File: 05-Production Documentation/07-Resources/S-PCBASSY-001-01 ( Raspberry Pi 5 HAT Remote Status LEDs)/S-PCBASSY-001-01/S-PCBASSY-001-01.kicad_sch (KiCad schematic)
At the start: 0 parts

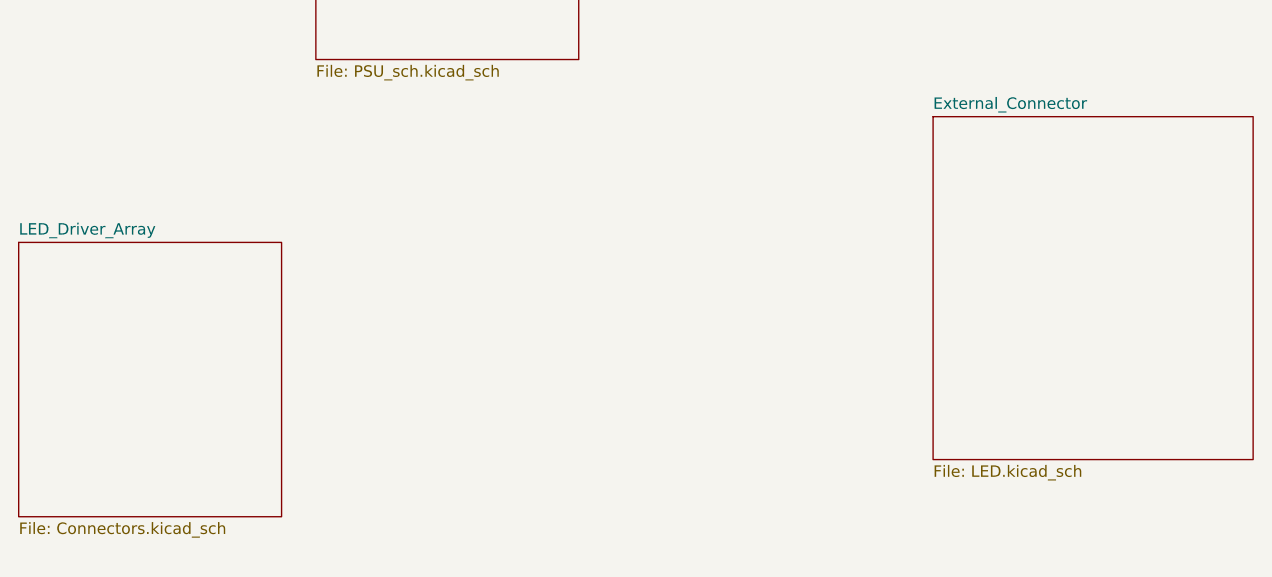
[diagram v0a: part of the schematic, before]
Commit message: Connector added with TVS still need to add polarity Protection
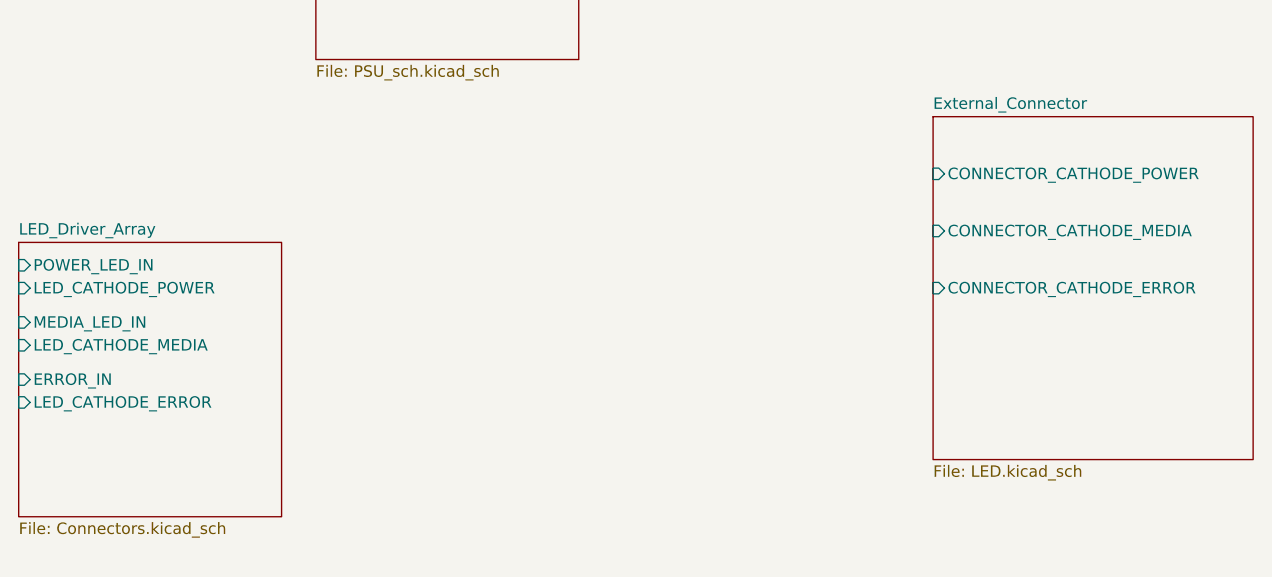
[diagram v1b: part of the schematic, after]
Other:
- sheet External_Connector ports: added CONNECTOR_CATHODE_ERROR, CONNECTOR_CATHODE_MEDIA, CONNECTOR_CATHODE_POWER; removed none
- sheet LED_Driver_Array ports: added ERROR_IN, LED_CATHODE_ERROR, LED_CATHODE_MEDIA, LED_CATHODE_POWER, MEDIA_LED_IN, POWER_LED_IN; removed none
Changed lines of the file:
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@@
+			)
+		)
+		(pin "LED_CATHODE_MEDIA" input
+			(at 97.79 104.14 180)
+			(effects
+				(font
+					(size 1.27 1.27)
+				)
+				(justify left)
+			)
+		)
+		(pin "MEDIA_LED_IN" input
+			(at 97.79 101.6 180)
+			(effects
+				(font
+					(size 1.27 1.27)
+				)
+				(justify left)
+			)
+		)
+		(pin "ERROR_IN" input
+			(at 97.79 107.95 180)
+			(effects
+				(font
+					(size 1.27 1.27)
+				)
+				(justify left)
+			)
+		)
+		(pin "LED_CATHODE_POWER" input
+			(at 97.79 97.79 180)
+			(effects
+				(font
+					(size 1.27 1.27)
+				)
+				(justify left)
+			)
+		)
+		(pin "LED_CATHODE_ERROR" input
+			(at 97.79 110.49 180)
+			(effects
+				(font
+					(size 1.27 1.27)
+				)
+				(justify left)
+			)
+		)
+		(pin "POWER_LED_IN" input
+			(at 97.79 95.25 180)
+			(effects
+				(font
+					(size 1.27 1.27)
+				)
+				(justify left)
 			)
 		)
@@
 			)
 		)
+		(pin "CONNECTOR_CATHODE_POWER" input
+			(at 199.39 85.09 180)
+			(effects
+				(font
+					(size 1.27 1.27)
+				)
+				(justify left)
+			)
+		)
+		(pin "CONNECTOR_CATHODE_MEDIA" input
+			(at 199.39 91.44 180)
+			(effects
+				(font
+					(size 1.27 1.27)
+				)
+				(justify left)
+			)
+		)
+		(pin "CONNECTOR_CATHODE_ERROR" input
+			(at 199.39 97.79 180)
+			(effects
+				(font
+					(size 1.27 1.27)
+				)
+				(justify left)
+			)
+		)

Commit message: Schematics done
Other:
- sheet RPi_Processor_Interface ports: added ERROR_RPi, MEDIA_LED_RPi, POWER_LED_RPi; removed none
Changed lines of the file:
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@@
+		)
+	)
+	(wire
+		(pts
+			(xy 139.7 83.82) (xy 144.78 83.82)
+		)
+		(stroke
+			(width 0)
+			(type default)
+		)
+	)
+	(wire
+		(pts
+			(xy 139.7 91.44) (xy 144.78 91.44)
+		)
+		(stroke
+			(width 0)
+			(type default)
+		)
+	)
+	(wire
+		(pts
+			(xy 191.77 87.63) (xy 199.39 87.63)
+		)
+		(stroke
+			(width 0)
+			(type default)
+		)
+	)
+	(wire
+		(pts
+			(xy 139.7 87.63) (xy 144.78 87.63)
+		)
+		(stroke
+			(width 0)
+			(type default)
+		)
+	)
+	(wire
+		(pts
+			(xy 191.77 91.44) (xy 199.39 91.44)
+		)
+		(stroke
+			(width 0)
+			(type default)
+		)
+	)
+	(wire
+		(pts
+			(xy 191.77 83.82) (xy 199.39 83.82)
+		)
+		(stroke
+			(width 0)
+			(type default)
 		)
 	)
 	(sheet
-		(at 130.81 45.72)
-		(size 29.21 26.67)
+		(at 110.49 78.74)
+		(size 29.21 17.78)
 		(exclude_from_sim no)
 		(in_bom yes)
@@
 			(width 0.1524)
 			(type solid)
+			(color 128 0 0 1)
 		)
 		(fill
-			(color 0 0 0 0.0000)
+			(color 128 255 128 1.0000)
 		)
 		(property "Sheetname" "RPi_Processor_Interface"
-			(at 130.81 45.0084 0)
+			(at 110.49 78.0284 0)
 			(effects
 				(font
@@
 		)
 		(property "Sheetfile" "PSU_sch.kicad_sch"
-			(at 130.81 72.9746 0)
+			(at 110.49 97.1046 0)
 			(effects
 				(font
@@
 				)
 				(justify left top)
+			)
+		)
+		(pin "ERROR_RPi" input
+			(at 139.7 91.44 0)
+			(effects
+				(font
+					(size 1.27 1.27)
+				)
+				(justify right)
+			)
+		)
+		(pin "MEDIA_LED_RPi" input
+			(at 139.7 87.63 0)
+			(effects
+				(font
+					(size 1.27 1.27)
+				)
+				(justify right)
+			)
+		)
+		(pin "POWER_LED_RPi" input
+			(at 139.7 83.82 0)
+			(effects
+				(font
+					(size 1.27 1.27)
+				)
+				(justify right)
 			)
 		)
@@
 	)
 	(sheet
-		(at 97.79 92.71)
-		(size 29.21 30.48)
+		(at 144.78 78.74)
+		(size 46.99 17.78)
 		(exclude_from_sim no)
 		(in_bom yes)
@@
 		)
 		(fill
-			(color 0 0 0 0.0000)
+			(color 128 255 128 1.0000)
 		)
 		(property "Sheetname" "LED_Driver_Array"
-			(at 97.79 91.9984 0)
+			(at 144.78 78.0284 0)
 			(effects
 				(font
@@
 		)
 		(property "Sheetfile" "Connectors.kicad_sch"
-			(at 97.79 123.7746 0)
+			(at 144.78 97.1046 0)
 			(effects
 				(font
@@
 		)
 		(pin "LED_CATHODE_MEDIA" input
-			(at 97.79 104.14 180)
-			(effects
-				(font
-					(size 1.27 1.27)
-				)
-				(justify left)
+			(at 191.77 87.63 0)
+			(effects
+				(font
+					(size 1.27 1.27)
+				)
+				(justify right)
 			)
 		)
 		(pin "MEDIA_LED_IN" input
-			(at 97.79 101.6 180)
+			(at 144.78 87.63 180)
 			(effects
 				(font
@@
 		)
 		(pin "ERROR_IN" input
-			(at 97.79 107.95 180)
+			(at 144.78 91.44 180)
 			(effects
 				(font
@@
 		)
 		(pin "LED_CATHODE_POWER" input
-			(at 97.79 97.79 180)
-			(effects
-				(font
-					(size 1.27 1.27)
-				)
-				(justify left)
+			(at 191.77 83.82 0)
+			(effects
+				(font
+					(size 1.27 1.27)
+				)
+				(justify right)
 			)
 		)
 		(pin "LED_CATHODE_ERROR" input
-			(at 97.79 110.49 180)
-			(effects
-				(font
-					(size 1.27 1.27)
-				)
-				(justify left)
+			(at 191.77 91.44 0)
+			(effects
+				(font
+					(size 1.27 1.27)
+				)
+				(justify right)
 			)
 		)
 		(pin "POWER_LED_IN" input
-			(at 97.79 95.25 180)
+			(at 144.78 83.82 180)
 			(effects
 				(font
@@
 	(sheet
 		(at 199.39 78.74)
-		(size 35.56 38.1)
+		(size 35.56 17.78)
 		(exclude_from_sim no)
 		(in_bom yes)
@@
 		)
 		(fill
-			(color 0 0 0 0.0000)
+			(color 128 255 128 1.0000)
 		)
 		(property "Sheetname" "External_Connector"
@@
 		)
 		(property "Sheetfile" "LED.kicad_sch"
-			(at 199.39 117.4246 0)
+			(at 199.39 97.1046 0)
 			(effects
 				(font
@@
 		)
 		(pin "CONNECTOR_CATHODE_POWER" input
-			(at 199.39 85.09 180)
+			(at 199.39 83.82 180)
 			(effects
 				(font
@@
 		)
 		(pin "CONNECTOR_CATHODE_MEDIA" input
+			(at 199.39 87.63 180)
+			(effects
+				(font
+					(size 1.27 1.27)
+				)
+				(justify left)
+			)
+		)
+		(pin "CONNECTOR_CATHODE_ERROR" input
 			(at 199.39 91.44 180)
 			(effects
 				(font
-					(size 1.27 1.27)
-				)
-				(justify left)
-			)
-		)
-		(pin "CONNECTOR_CATHODE_ERROR" input
-			(at 199.39 97.79 180)
-			(effects
-				(font

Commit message: ERC Completed and passed
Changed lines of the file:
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@@
 	(wire
 		(pts
-			(xy 139.7 83.82) (xy 144.78 83.82)
-		)
-		(stroke
-			(width 0)
-			(type default)
-		)
-	)
-	(wire
-		(pts
-			(xy 139.7 91.44) (xy 144.78 91.44)
-		)
-		(stroke
-			(width 0)
-			(type default)
-		)
-	)
-	(wire
-		(pts
-			(xy 191.77 87.63) (xy 199.39 87.63)
-		)
-		(stroke
-			(width 0)
-			(type default)
-		)
-	)
-	(wire
-		(pts
-			(xy 139.7 87.63) (xy 144.78 87.63)
-		)
-		(stroke
-			(width 0)
-			(type default)
-		)
-	)
-	(wire
-		(pts
-			(xy 191.77 91.44) (xy 199.39 91.44)
-		)
-		(stroke
-			(width 0)
-			(type default)
-		)
-	)
-	(wire
-		(pts
-			(xy 191.77 83.82) (xy 199.39 83.82)
+			(xy 119.38 90.17) (xy 124.46 90.17)
+		)
+		(stroke
+			(width 0)
+			(type default)
+		)
+	)
+	(wire
+		(pts
+			(xy 119.38 97.79) (xy 124.46 97.79)
+		)
+		(stroke
+			(width 0)
+			(type default)
+		)
+	)
+	(wire
+		(pts
+			(xy 171.45 93.98) (xy 179.07 93.98)
+		)
+		(stroke
+			(width 0)
+			(type default)
+		)
+	)
+	(wire
+		(pts
+			(xy 119.38 93.98) (xy 124.46 93.98)
+		)
+		(stroke
+			(width 0)
+			(type default)
+		)
+	)
+	(wire
+		(pts
+			(xy 171.45 97.79) (xy 179.07 97.79)
+		)
+		(stroke
+			(width 0)
+			(type default)
+		)
+	)
+	(wire
+		(pts
+			(xy 171.45 90.17) (xy 179.07 90.17)
 		)
 		(stroke
@@
 	)
 	(sheet
-		(at 110.49 78.74)
+		(at 90.17 85.09)
 		(size 29.21 17.78)
 		(exclude_from_sim no)
@@
 		)
 		(property "Sheetname" "RPi_Processor_Interface"
-			(at 110.49 78.0284 0)
+			(at 90.17 84.3784 0)
 			(effects
 				(font
@@
 		)
 		(property "Sheetfile" "PSU_sch.kicad_sch"
-			(at 110.49 97.1046 0)
+			(at 90.17 103.4546 0)
 			(effects
 				(font
@@
 		)
 		(pin "ERROR_RPi" input
-			(at 139.7 91.44 0)
+			(at 119.38 97.79 0)
 			(effects
 				(font
@@
 		)
 		(pin "MEDIA_LED_RPi" input
-			(at 139.7 87.63 0)
+			(at 119.38 93.98 0)
 			(effects
 				(font
@@
 		)
 		(pin "POWER_LED_RPi" input
-			(at 139.7 83.82 0)
+			(at 119.38 90.17 0)
 			(effects
 				(font
@@
 	)
 	(sheet
-		(at 144.78 78.74)
+		(at 124.46 85.09)
 		(size 46.99 17.78)
 		(exclude_from_sim no)
@@
 		)
 		(property "Sheetname" "LED_Driver_Array"
-			(at 144.78 78.0284 0)
+			(at 124.46 84.3784 0)
 			(effects
 				(font
@@
 		)
 		(property "Sheetfile" "Connectors.kicad_sch"
-			(at 144.78 97.1046 0)
+			(at 124.46 103.4546 0)
 			(effects
 				(font
@@
 		)
 		(pin "LED_CATHODE_MEDIA" input
-			(at 191.77 87.63 0)
+			(at 171.45 93.98 0)
 			(effects
 				(font
@@
 		)
 		(pin "MEDIA_LED_IN" input
-			(at 144.78 87.63 180)
+			(at 124.46 93.98 180)
 			(effects
 				(font
@@
 		)
 		(pin "ERROR_IN" input
-			(at 144.78 91.44 180)
+			(at 124.46 97.79 180)
 			(effects
 				(font
@@
 		)
 		(pin "LED_CATHODE_POWER" input
-			(at 191.77 83.82 0)
+			(at 171.45 90.17 0)
 			(effects
 				(font
@@
 		)
 		(pin "LED_CATHODE_ERROR" input
-			(at 191.77 91.44 0)
+			(at 171.45 97.79 0)
 			(effects
 				(font
@@
 		)
 		(pin "POWER_LED_IN" input
-			(at 144.78 83.82 180)
+			(at 124.46 90.17 180)
 			(effects
 				(font
@@
 	)
 	(sheet
-		(at 199.39 78.74)
+		(at 179.07 85.09)
 		(size 35.56 17.78)
 		(exclude_from_sim no)
@@
 		)
 		(property "Sheetname" "External_Connector"
-			(at 199.39 78.0284 0)
+			(at 179.07 84.3784 0)
 			(effects
 				(font
@@
 		)
 		(property "Sheetfile" "LED.kicad_sch"
-			(at 199.39 97.1046 0)
+			(at 179.07 103.4546 0)
 			(effects
 				(font
@@
 		)
 		(pin "CONNECTOR_CATHODE_POWER" input
-			(at 199.39 83.82 180)
+			(at 179.07 90.17 180)
 			(effects
 				(font
@@
 		)
 		(pin "CONNECTOR_CATHODE_MEDIA" input
-			(at 199.39 87.63 180)
+			(at 179.07 93.98 180)
 			(effects
 				(font
@@
 		)
 		(pin "CONNECTOR_CATHODE_ERROR" input
-			(at 199.39 91.44 180)
-			(effects
-				(font
+			(at 179.07 97.79 180)
+			(effects
+				(font
